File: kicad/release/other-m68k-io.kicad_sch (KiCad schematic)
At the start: 19 parts, among them J2 FTDI (GND CTS VCC TXD RXD RTS), J8 Expansion, SW1 RESET, U10 MC68681P, U13 MCP130T-450I/TT, Y1 3.6864MHz

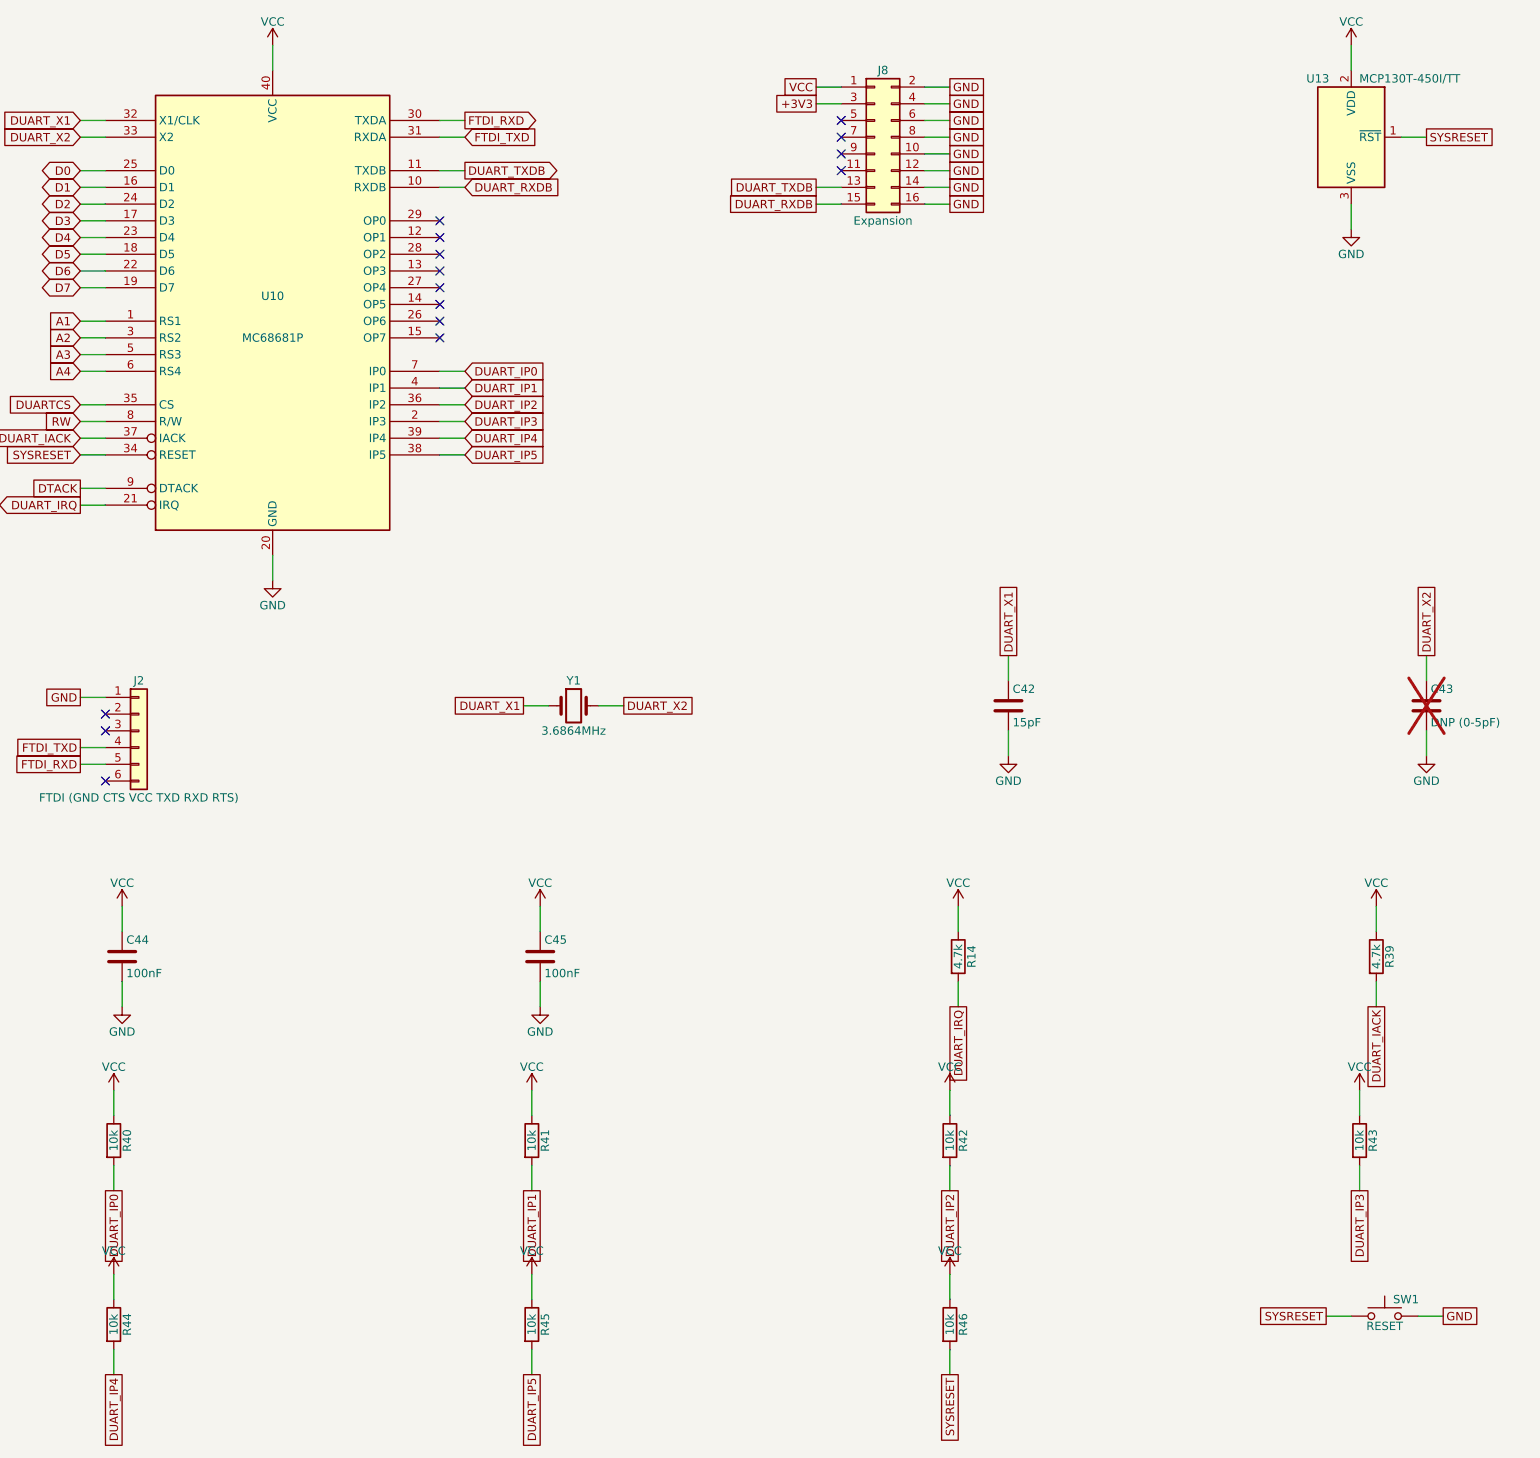
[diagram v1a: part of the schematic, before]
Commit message: board rev C2 (spec rev 10): front and back edges, S-video jack, serial B header, dedication silkscreen
The rev B4 order was stopped; rev C2 is what goes to PCBWay. The sheet's bottom edge is the
machine's front: J3 PS/2, J6 audio, J4 microSD (LDO behind it), then SW1 RESET and SW2 NMI
with the LEDs D5 PWR, D3 LED0, D4 LED1 behind them, all labelled. The top edge is the back:
J1 USB-C, J2 serial A, J11 serial B (a second FTDI-pinout header on DUART channel B; it
replaces the 2x8 expansion header J8, which carried only channel B and the rails after spec
rev 7), J5 composite, J10 S-video (CUI MD-40SM mini-DIN 4 on the AD724's LUMA and CRMA
outputs through 220 uF and 75 ohm each; new footprint and symbol in kicad/lib). J9 (logic
analyzer) and J7 (JTAG) stand on the left edge with the six series arrays hand-placed in a
spaced column (the auto-placed cluster left one connection unroutable). The flash chips
stand vertically at the right edge; the AD724 section sits right of the S-video jack; the
bus buffers moved under the SRAMs. The open area under the CPU carries "Griffin Jr.",
"October 2026", "I love you, Kris!" and the revision; connector labels are placed where
the silkscreen checker finds them free of pads and other silk.

Routed by freerouting (optimizer on): 0 DRC violations, 0 unrouted. Fab package and
release regenerated; ORDER.md rewritten for rev C2. Spec rev 10 carries only the connector
wording (serial headers, S-video); no register or firmware change.

Co-Authored-By: Claude Fable 5.1 <noreply@anthropic.com>
Claude-Session: https://claude.ai/code/session_019bbFLKMxhKXGW6aABP44Z1
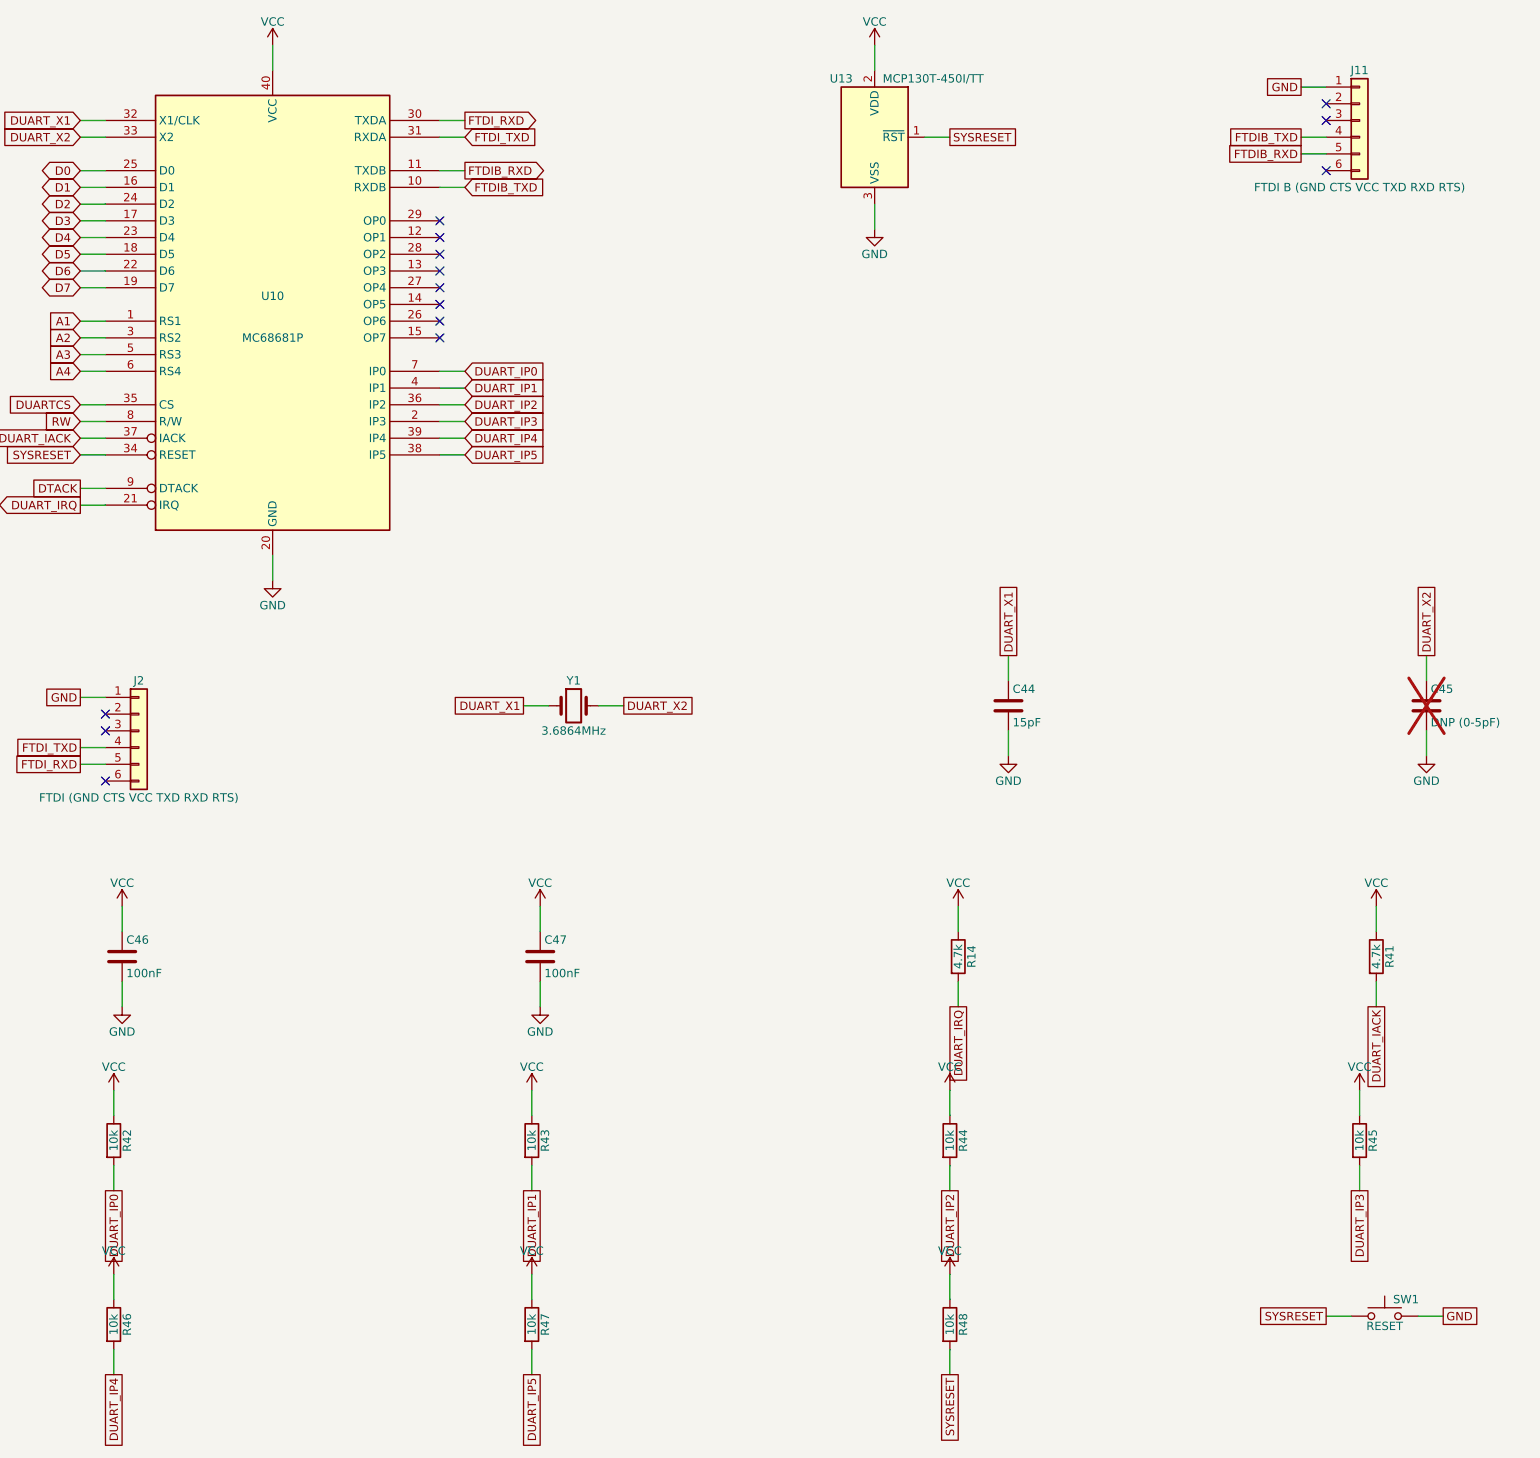
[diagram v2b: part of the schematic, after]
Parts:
- removed C42: 15pF, Capacitor_SMD:C_0603_1608Metric, symbol Device:C
- removed C43: DNP (0-5pF), Capacitor_SMD:C_0603_1608Metric, symbol Device:C
- removed J8: Expansion, Connector_PinHeader_2.54mm:PinHeader_2x08_P2.54mm_Vertical, symbol Connector_Generic:Conn_02x08_Odd_Even
- removed R39: 4.7k, Resistor_SMD:R_0603_1608Metric, symbol Device:R
- removed R40: 10k, Resistor_SMD:R_0603_1608Metric, symbol Device:R
- added C46, C47: 100nF, Capacitor_SMD:C_0603_1608Metric, symbol Device:C
- added J11: FTDI B (GND CTS VCC TXD RXD RTS), Connector_PinHeader_2.54mm:PinHeader_1x06_P2.54mm_Vertical, symbol Connector_Generic:Conn_01x06
- added R47, R48: 10k, Resistor_SMD:R_0603_1608Metric, symbol Device:R
- C44: value 100nF -> 15pF; Desc 100 nF 50 V X7R 0603 -> 15 pF 50 V C0G 0603; LCSC C1591 -> C1644; MPN CL10B104KB8NNNC -> CL10C150JB8NNNC; PcbNear U10 -> Y1
- C45: value 100nF -> DNP (0-5pF); Assembly pcba -> dnp; Desc 100 nF 50 V X7R 0603 -> not fitted (crystal trim); LCSC C1591 -> (none); MPN CL10B104KB8NNNC -> (none); Manufacturer Samsung -> (none); PcbNear U13 -> Y1; now not fitted
- R41: value 10k -> 4.7k; Desc 10 k 1% 0603 -> 4.7 k 1% 0603; LCSC C25804 -> C23162; MPN RC0603FR-0710KL -> RC0603FR-074K7L
- R46: PcbNear U13 -> U10
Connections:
- net DUART_IACK: now also R41.2
- net DUART_IP0: now also R42.2
- net DUART_IP1: now also R43.2; no longer R41.2
- net DUART_IP2: now also R44.2; no longer R42.2
- net DUART_IP3: now also R45.2; no longer R43.2
- net DUART_IP4: now also R46.2; no longer R44.2
- net DUART_IP5: now also R47.2; no longer R45.2
- net DUART_X1: now also C44.1
- net DUART_X2: now also C45.1
- net GND: now also C46.2, C47.2, J11.1 (Pin_1)
- net SYSRESET: now also R48.2; no longer R46.2
- net VCC: now also C46.1, C47.1, R47.1, R48.1; no longer C44.1, C45.1
- net DUART_RXDB renamed FTDIB_TXD
- net FTDIB_TXD: now also J11.4 (Pin_4)
- net DUART_TXDB renamed FTDIB_RXD
- net FTDIB_RXD: now also J11.5 (Pin_5)
- no-connect marks 15 -> 14
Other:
- moved on the sheet: C44, R41, R42, R43, R44, R45, R46, U13
